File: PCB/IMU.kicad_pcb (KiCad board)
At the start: 2 copper layers, 65 parts, among them IC1 STM32F405VGT, IC2 ADP3335ARMZ-3.3, IC3 ADP3335ARMZ-5, IC4 MS5611-01BA03, P1 UART1, P2 SWD, P3 UART2, P4 SPI, P5 BATTERY, P6 3V3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

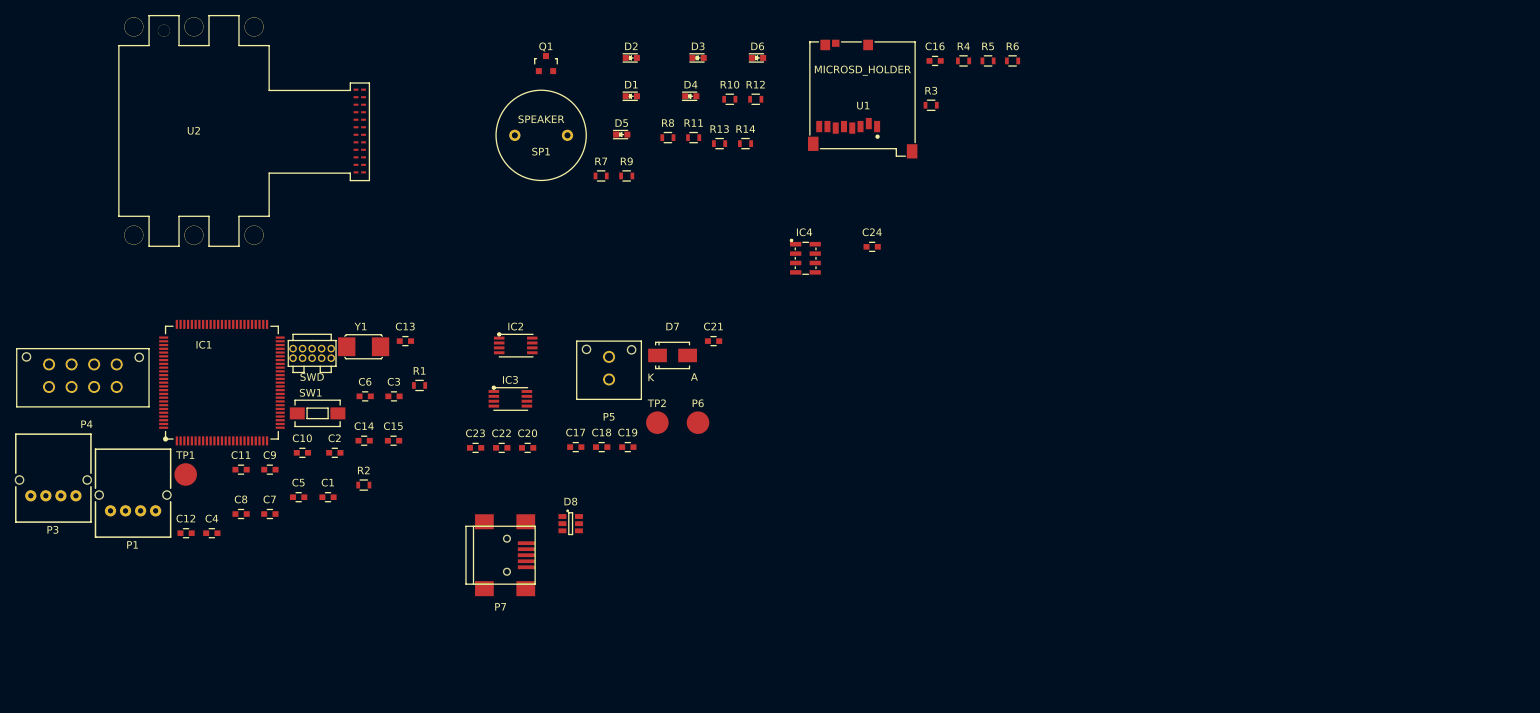
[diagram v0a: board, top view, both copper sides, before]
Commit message: PCB: place components around STM32
Those components whose placing is required to be close to particular pads have
been placed and routed.
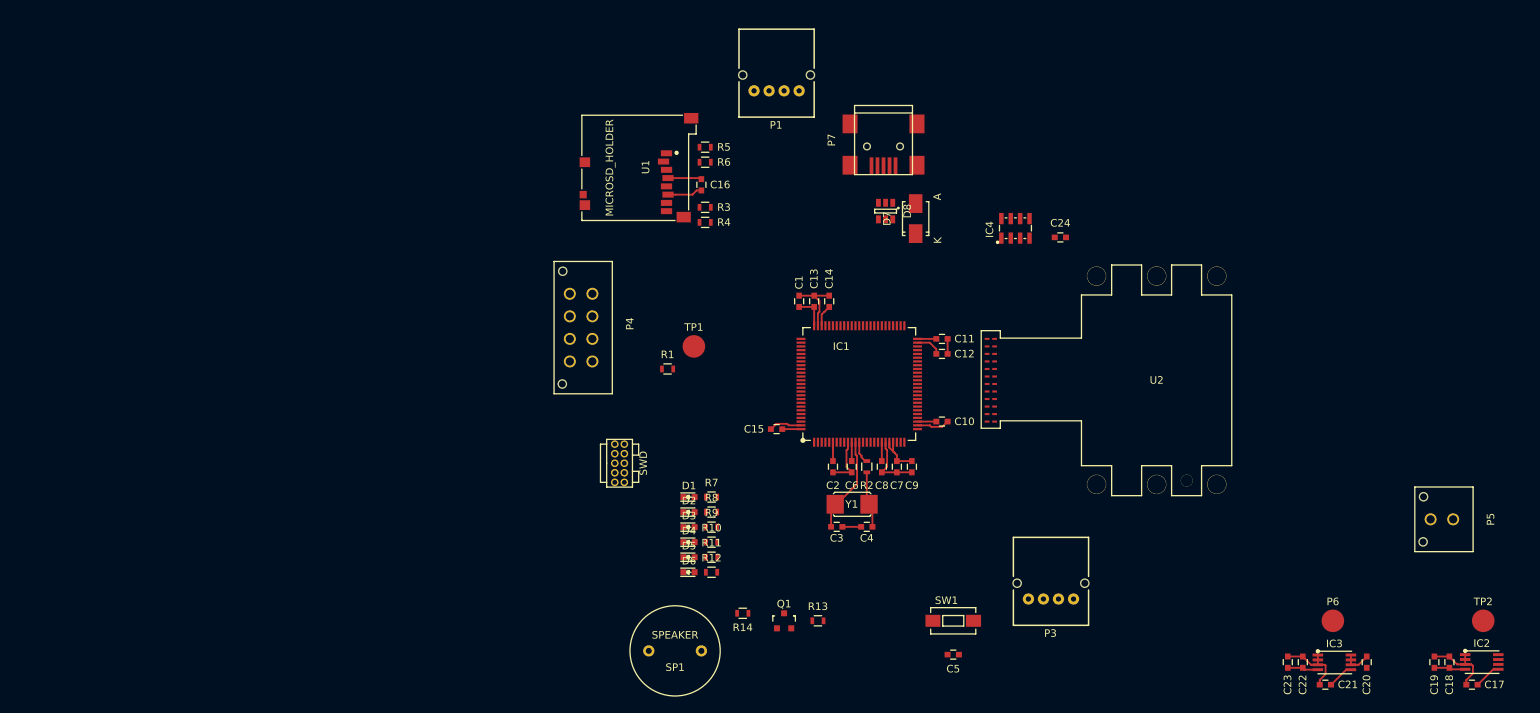
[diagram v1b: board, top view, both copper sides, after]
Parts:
- moved U2 174.6 mm to (243.6, 97.0), turned to 180 degrees
- moved IC2 135.2 mm to (262.1, 139.0)
- moved P3 133.4 mm to (204.0, 131.6)
- moved C17 123.3 mm to (263.0, 143.0)
- moved C18 116.3 mm to (260.0, 140.0), turned to 270 degrees
- moved C20 115.2 mm to (249.0, 140.0), turned to 270 degrees
- moved IC3 115.1 mm to (242.5, 139.1)
- moved P5 113.8 mm to (260.5, 121.0), turned to 90 degrees
- moved TP2 113.0 mm to (264.5, 134.5)
- moved C23 111.7 mm to (238.5, 140.0), turned to 270 degrees
- moved C19 111.0 mm to (258.0, 140.0), turned to 270 degrees
- moved C22 110.3 mm to (240.5, 140.0), turned to 270 degrees
- moved C12 103.3 mm to (192.5, 99.0)
- moved P1 102.2 mm to (167.5, 64.0)
- moved C11 94.8 mm to (192.5, 97.0)
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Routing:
- net GND: track 0.00 -> 49.8 mm
- net +3V3: track 0.00 -> 40.3 mm
- net Net-(C3-Pad1): track 0.00 -> 12.8 mm
- net +5V: track 0.00 -> 9.71 mm
- net Net-(C4-Pad1): track 0.00 -> 7.56 mm
- net +BATT: track 0.00 -> 3.87 mm
- net Net-(C17-Pad2): track 0.00 -> 3.60 mm
- net Net-(C12-Pad1): track 0.00 -> 3.49 mm
- net Net-(C21-Pad2): track 0.00 -> 3.48 mm
- net Net-(IC1-Pad13): track 0.00 -> 3.03 mm
- net Net-(C14-Pad1): track 0.00 -> 2.93 mm

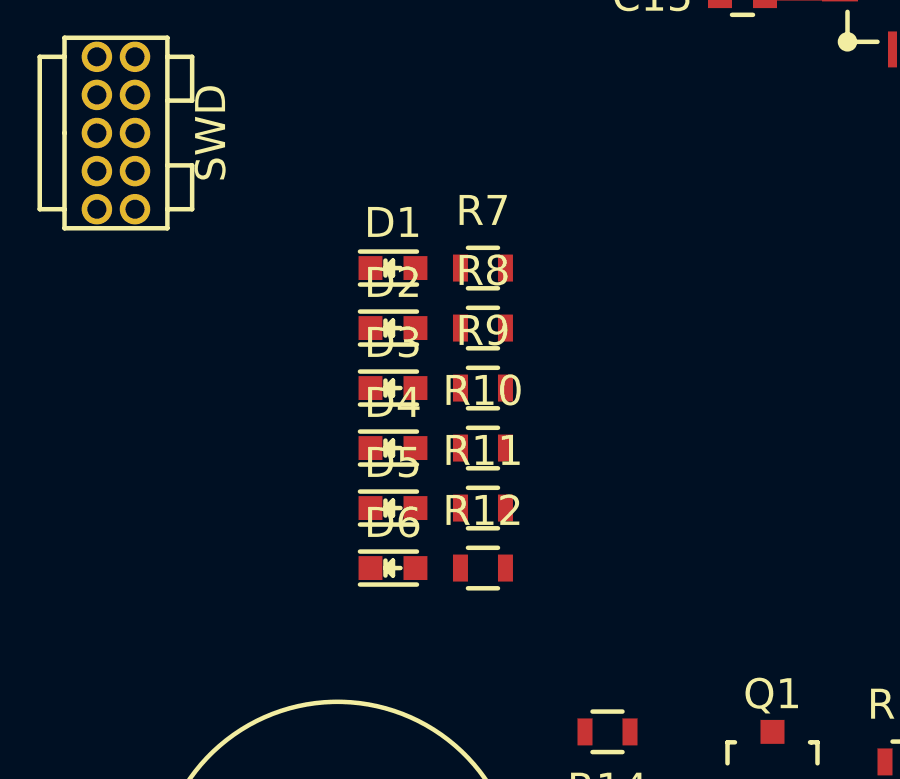
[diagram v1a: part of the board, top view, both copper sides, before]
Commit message: PCB: align D1-6 with 0.5mm grid
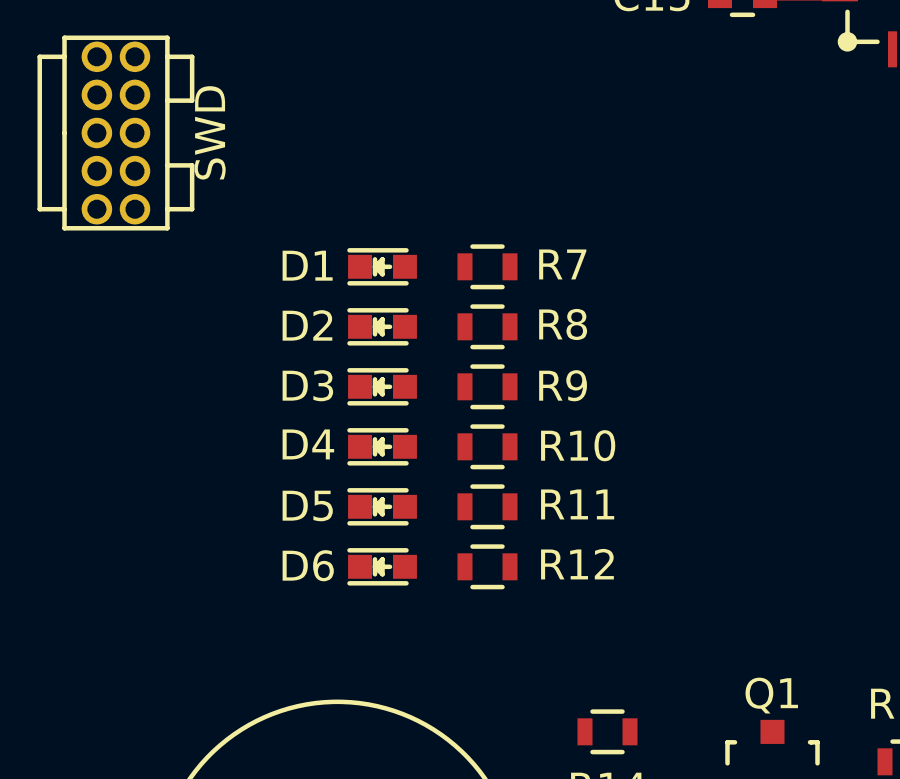
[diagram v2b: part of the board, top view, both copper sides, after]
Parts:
- moved D6 0.35 mm to (158.5, 128.0)
- moved D1 0.35 mm to (158.5, 118.0)
- moved D2 0.35 mm to (158.5, 120.0)
- moved D3 0.35 mm to (158.5, 122.0)
- moved D4 0.35 mm to (158.5, 124.0)
- moved D5 0.35 mm to (158.5, 126.0)
- moved R12 0.16 mm to (162.0, 128.0)
- moved R10 0.16 mm to (162.0, 124.0)
- moved R11 0.16 mm to (162.0, 126.0)
- moved R7 0.16 mm to (162.0, 118.0)
- moved R8 0.16 mm to (162.0, 120.0)
- moved R9 0.16 mm to (162.0, 122.0)
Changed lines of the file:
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@@
   (general
     (links 181)
-    (no_connects 181)
-    (area 85.475 55.499999 263.0698 144.775001)
+    (no_connects 130)
+    (area 136.875 55.499999 271.994048 145.875)
     (thickness 1.6)
     (drawings 0)
@@
   )
   (module LEDs:LED-0603 (layer F.Cu)
-    (at 158.849098 118.041162)
+    (at 158.5 118)
     (descr "LED 0603 smd package")
     (tags "LED led 0603 SMD smd SMT smt smdled SMDLED smtled SMTLED")
     (attr smd)
-    (fp_text reference D1 (at 0 -1.5) (layer F.SilkS)
+    (fp_text reference D1 (at -2.5 0) (layer F.SilkS)
       (effects (font (size 1 1) (thickness 0.15)))
     )
@@
   )
   (module LEDs:LED-0603 (layer F.Cu)
-    (at 158.849098 120.041162)
+    (at 158.5 120)
     (descr "LED 0603 smd package")
     (tags "LED led 0603 SMD smd SMT smt smdled SMDLED smtled SMTLED")
     (attr smd)
-    (fp_text reference D2 (at 0 -1.5) (layer F.SilkS)
+    (fp_text reference D2 (at -2.5 0) (layer F.SilkS)
       (effects (font (size 1 1) (thickness 0.15)))
     )
@@
   )
   (module LEDs:LED-0603 (layer F.Cu)
-    (at 158.849098 122.041162)
+    (at 158.5 122)
     (descr "LED 0603 smd package")
     (tags "LED led 0603 SMD smd SMT smt smdled SMDLED smtled SMTLED")
     (attr smd)
-    (fp_text reference D3 (at 0 -1.5) (layer F.SilkS)
+    (fp_text reference D3 (at -2.5 0) (layer F.SilkS)
       (effects (font (size 1 1) (thickness 0.15)))
     )
@@
   )
   (module LEDs:LED-0603 (layer F.Cu)
-    (at 158.849098 124.041162)
+    (at 158.5 124)
     (descr "LED 0603 smd package")
     (tags "LED led 0603 SMD smd SMT smt smdled SMDLED smtled SMTLED")
     (attr smd)
-    (fp_text reference D4 (at 0 -1.5) (layer F.SilkS)
+    (fp_text reference D4 (at -2.5 -0.041162) (layer F.SilkS)
       (effects (font (size 1 1) (thickness 0.15)))
     )
@@
   )
   (module LEDs:LED-0603 (layer F.Cu)
-    (at 158.849098 126.041162)
+    (at 158.5 126)
     (descr "LED 0603 smd package")
     (tags "LED led 0603 SMD smd SMT smt smdled SMDLED smtled SMTLED")
     (attr smd)
-    (fp_text reference D5 (at 0 -1.5) (layer F.SilkS)
+    (fp_text reference D5 (at -2.5 0) (layer F.SilkS)
       (effects (font (size 1 1) (thickness 0.15)))
     )
@@
   )
   (module LEDs:LED-0603 (layer F.Cu)
-    (at 158.849098 128.041162)
+    (at 158.5 128)
     (descr "LED 0603 smd package")
     (tags "LED led 0603 SMD smd SMT smt smdled SMDLED smtled SMTLED")
     (attr smd)
-    (fp_text reference D6 (at 0 -1.5) (layer F.SilkS)
+    (fp_text reference D6 (at -2.5 0) (layer F.SilkS)
       (effects (font (size 1 1) (thickness 0.15)))
     )
@@
   )
   (module Resistors_SMD:R_0603 (layer F.Cu)
-    (at 161.849098 118.041162)
+    (at 162 118)
     (descr "Resistor SMD 0603, reflow soldering, Vishay (see dcrcw.pdf)")
     (tags "resistor 0603")
     (attr smd)
-    (fp_text reference R7 (at 0 -1.9) (layer F.SilkS)
+    (fp_text reference R7 (at 2.5 -0.041162) (layer F.SilkS)
       (effects (font (size 1 1) (thickness 0.15)))
     )
@@
   )
   (module Resistors_SMD:R_0603 (layer F.Cu)
-    (at 161.849098 120.041162)
+    (at 162 120)
     (descr "Resistor SMD 0603, reflow soldering, Vishay (see dcrcw.pdf)")
     (tags "resistor 0603")
     (attr smd)
-    (fp_text reference R8 (at 0 -1.9) (layer F.SilkS)
+    (fp_text reference R8 (at 2.5 -0.041162) (layer F.SilkS)
       (effects (font (size 1 1) (thickness 0.15)))
     )
@@
   )
   (module Resistors_SMD:R_0603 (layer F.Cu)
-    (at 161.849098 122.041162)
+    (at 162 122)
     (descr "Resistor SMD 0603, reflow soldering, Vishay (see dcrcw.pdf)")
     (tags "resistor 0603")
     (attr smd)
-    (fp_text reference R9 (at 0 -1.9) (layer F.SilkS)
+    (fp_text reference R9 (at 2.5 0) (layer F.SilkS)
       (effects (font (size 1 1) (thickness 0.15)))
     )
@@
   )
   (module Resistors_SMD:R_0603 (layer F.Cu)
-    (at 161.849098 124.041162)
+    (at 162 124)
     (descr "Resistor SMD 0603, reflow soldering, Vishay (see dcrcw.pdf)")
     (tags "resistor 0603")
     (attr smd)
-    (fp_text reference R10 (at 0 -1.9) (layer F.SilkS)
+    (fp_text reference R10 (at 3 0) (layer F.SilkS)
       (effects (font (size 1 1) (thickness 0.15)))
     )
@@
   )
   (module Resistors_SMD:R_0603 (layer F.Cu)
-    (at 161.849098 126.041162)
+    (at 162 126)
     (descr "Resistor SMD 0603, reflow soldering, Vishay (see dcrcw.pdf)")
     (tags "resistor 0603")
     (attr smd)
-    (fp_text reference R11 (at 0 -1.9) (layer F.SilkS)
+    (fp_text reference R11 (at 3 -0.041162) (layer F.SilkS)
       (effects (font (size 1 1) (thickness 0.15)))
     )
@@
   )
   (module Resistors_SMD:R_0603 (layer F.Cu)
-    (at 161.849098 128.041162)
+    (at 162 128)
     (descr "Resistor SMD 0603, reflow soldering, Vishay (see dcrcw.pdf)")
     (tags "resistor 0603")
     (attr smd)
-    (fp_text reference R12 (at 0 -1.9) (layer F.SilkS)
-      (effects (font (size 1 1) (thickness 0.15)))
-    )
+    (fp_text reference R12 (at 3 -0.041162) (layer F.SilkS)
+      (effects (font (size 1 1) (thickness 0.15)))
+    )

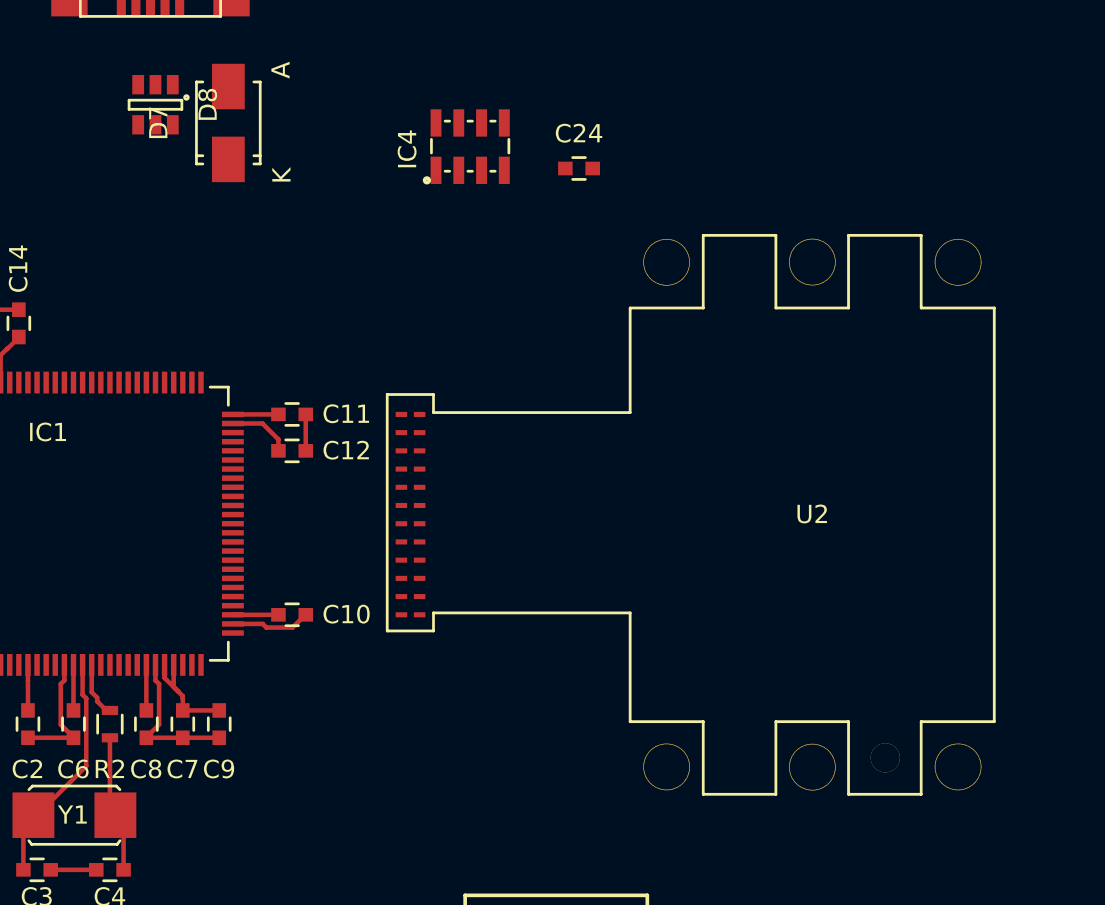
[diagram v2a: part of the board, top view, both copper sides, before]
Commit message: PCB: swap some GPIO pin assignment to improve layout
We have considerable freedom wrt GPIO pin locations. Route the inertial sensor's
data ready line to a useful side of the chip.
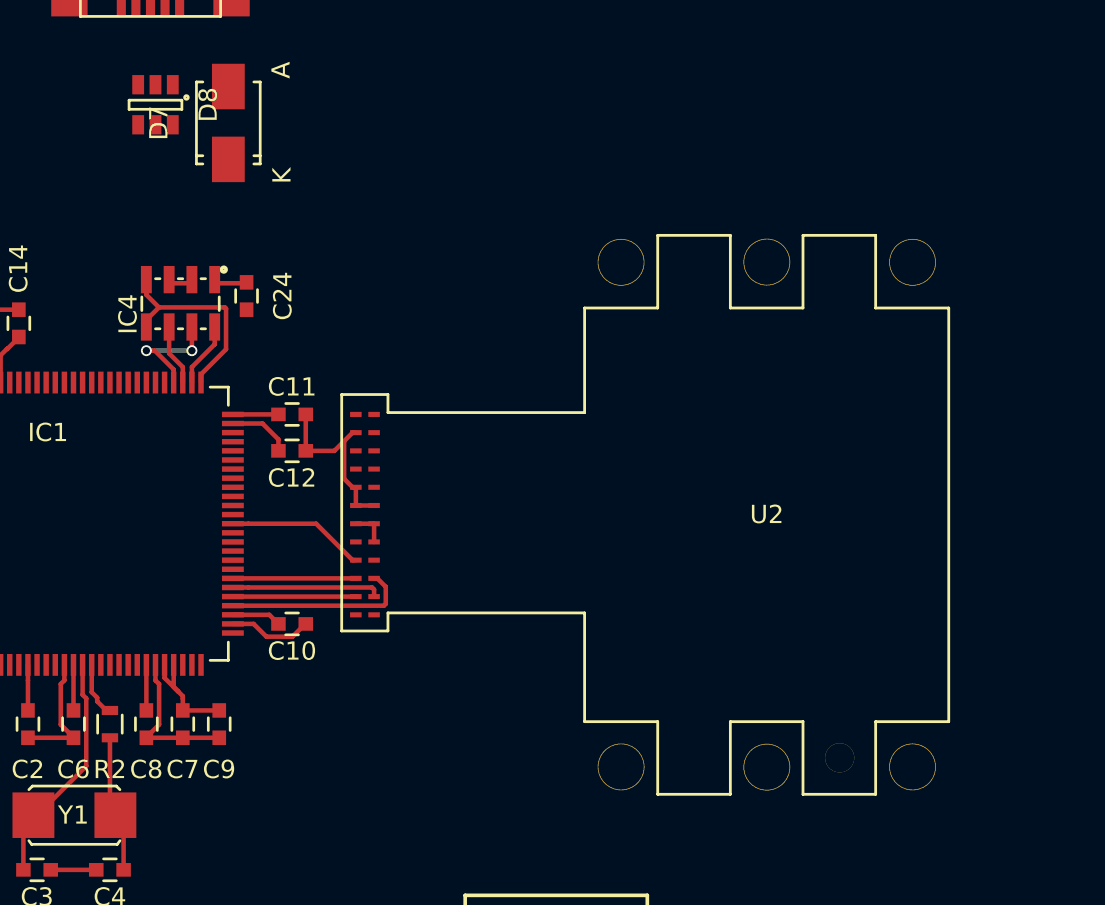
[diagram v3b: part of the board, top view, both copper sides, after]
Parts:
- moved C24 19.5 mm to (190.0, 90.5), turned to 270 degrees
- moved IC4 13.7 mm to (188.2, 89.8), turned to 270 degrees
- moved U2 2.50 mm to (241.1, 97.0)
- moved C10 0.50 mm to (192.5, 108.5)
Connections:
- IC1 pad 38: /DATA_RDY -> /IntertialSensors/IRQ
- IC1 pad 97: /IntertialSensors/IRQ -> /DATA_RDY
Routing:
- net SPI2_NSS: track 0.00 -> 11.1 mm
- net SPI1_NSS: track 0.00 -> 10.2 mm
- net GND: track 49.8 -> 59.3 mm
- net SPI1_MISO: track 0.00 -> 8.19 mm
- net /IntertialSensors/IRQ: track 0.00 -> 7.58 mm
- net SPI1_MOSI: track 0.00 -> 6.75 mm
- net SPI1_SCK: track 0.00 -> 6.75 mm
- net SPI2_MOSI: track 0.00 -> 6.64 mm, vias 0 -> 2
- net SPI2_SCK: track 0.00 -> 3.77 mm
- net SPI2_MISO: track 0.00 -> 3.56 mm
- net +5V: track 9.71 -> 11.7 mm
- net +3V3: track 40.3 -> 42.3 mm
